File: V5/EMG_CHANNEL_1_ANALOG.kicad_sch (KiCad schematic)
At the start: 38 parts, among them J301 AudioJack3 TRS, U301 INA333xxDGK, U302 MCP6004

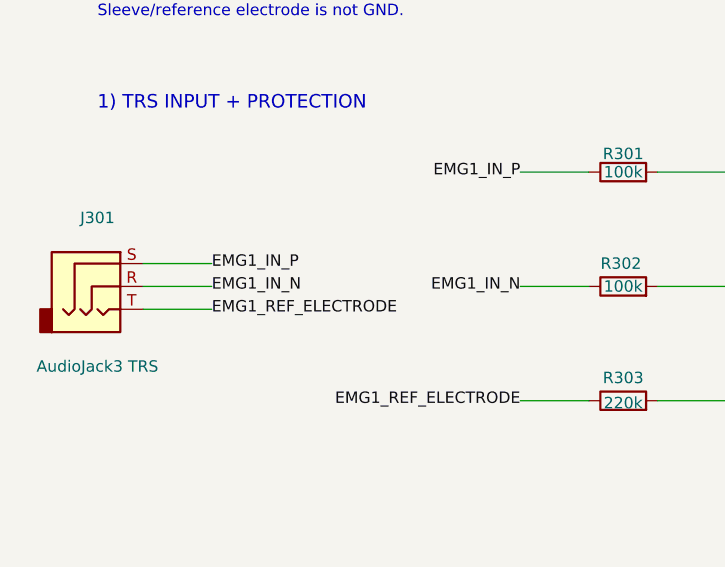
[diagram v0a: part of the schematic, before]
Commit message: fix trs electrode terminal mapping
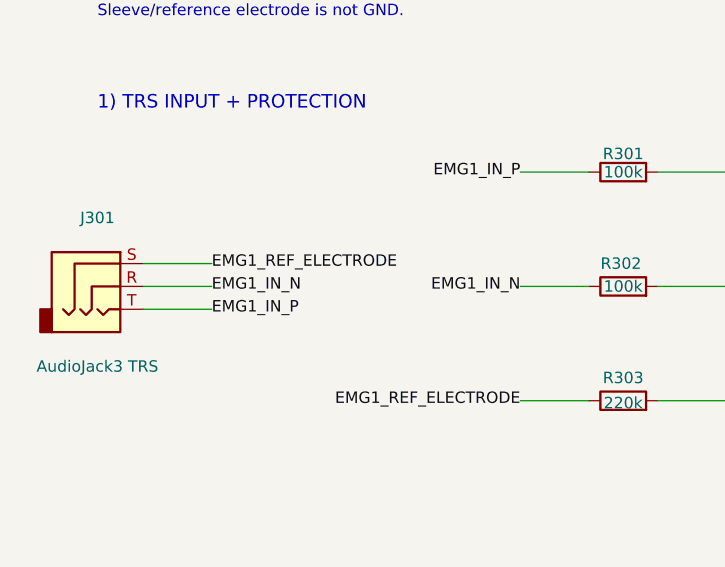
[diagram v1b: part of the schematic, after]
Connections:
- net EMG1_IN_P: now also J301.T; no longer J301.S
- net EMG1_REF_ELECTRODE: now also J301.S; no longer J301.T
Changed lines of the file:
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@@
 		)
 	)
-	(label "EMG1_IN_P"
+	(label "EMG1_REF_ELECTRODE"
 		(at 38.1 66.04 0)
 		(effects
@@
 		)
 	)
-	(label "EMG1_REF_ELECTRODE"
+	(label "EMG1_IN_P"
 		(at 38.1 71.12 0)
 		(effects

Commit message: assign mirrored analog footprint batch
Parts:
- C310, C311, C314: footprint (none) -> Capacitor_SMD:C_0603_1608Metric
- R311, R312, R313, R314, R321, R331, R341, R351: footprint (none) -> Resistor_SMD:R_0805_2012Metric
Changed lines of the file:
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@@
 			)
 		)
-		(property "Footprint" ""
+		(property "Footprint" "Capacitor_SMD:C_0603_1608Metric"
 			(at 195.58 58.42 0)
 			(hide yes)
@@
 			)
 		)
-		(property "Footprint" ""
+		(property "Footprint" "Capacitor_SMD:C_0603_1608Metric"
 			(at 246.38 73.66 0)
 			(hide yes)
@@
 			)
 		)
-		(property "Footprint" ""
+		(property "Footprint" "Resistor_SMD:R_0805_2012Metric"
 			(at 292.1 88.9 0)
 			(hide yes)
@@
 			)
 		)
-		(property "Footprint" ""
+		(property "Footprint" "Resistor_SMD:R_0805_2012Metric"
 			(at 302.26 107.95 0)
 			(hide yes)
@@
 			)
 		)
-		(property "Footprint" ""
+		(property "Footprint" "Resistor_SMD:R_0805_2012Metric"
 			(at 322.58 55.88 0)
 			(hide yes)
@@
 			)
 		)
-		(property "Footprint" ""
+		(property "Footprint" "Resistor_SMD:R_0805_2012Metric"
 			(at 365.76 73.66 0)
 			(hide yes)
@@
 			)
 		)
-		(property "Footprint" ""
+		(property "Footprint" "Capacitor_SMD:C_0603_1608Metric"
 			(at 434.34 78.74 0)
 			(hide yes)
@@
 			)
 		)
-		(property "Footprint" ""
+		(property "Footprint" "Resistor_SMD:R_0805_2012Metric"
 			(at 274.32 229.87 0)
 			(hide yes)
@@
 			)
 		)
-		(property "Footprint" ""
+		(property "Footprint" "Resistor_SMD:R_0805_2012Metric"
 			(at 438.15 57.15 0)
 			(hide yes)
@@
 			)
 		)
-		(property "Footprint" ""
+		(property "Footprint" "Resistor_SMD:R_0805_2012Metric"
 			(at 439.42 93.98 0)
 			(hide yes)
@@
 			)
 		)
-		(property "Footprint" ""
+		(property "Footprint" "Resistor_SMD:R_0805_2012Metric"
 			(at 436.88 119.38 0)
 			(hide yes)

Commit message: select and assign analog ic packages
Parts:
- U301: value INA333xxDGK -> INA333AIDGKT; footprint (none) -> Package_SO:VSSOP-8_3x3mm_P0.65mm
- U302: value MCP6004 -> MCP6004-I/SL; footprint Package_DIP:DIP-14_W7.62mm -> Package_SO:SOIC-14_3.9x8.7mm_P1.27mm
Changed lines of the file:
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@@
 			)
 		)
-		(property "Value" "INA333xxDGK"
+		(property "Value" "INA333AIDGKT"
 			(at 196.85 90.17 0)
 			(show_name no)
@@
 			)
 		)
-		(property "Footprint" ""
+		(property "Footprint" "Package_SO:VSSOP-8_3x3mm_P0.65mm"
 			(at 210.82 73.66 0)
 			(hide yes)
@@
 			)
 		)
-		(property "Value" "MCP6004"
+		(property "Value" "MCP6004-I/SL"
 			(at 322.58 80.518 0)
 			(show_name no)
@@
 			)
 		)
-		(property "Footprint" "Package_DIP:DIP-14_W7.62mm"
+		(property "Footprint" "Package_SO:SOIC-14_3.9x8.7mm_P1.27mm"
 			(at 322.58 73.66 0)
 			(hide yes)
@@
 			)
 		)
-		(property "Value" "MCP6004"
+		(property "Value" "MCP6004-I/SL"
 			(at 337.82 165.1 0)
 			(show_name no)
@@
 			)
 		)
-		(property "Footprint" "Package_DIP:DIP-14_W7.62mm"
+		(property "Footprint" "Package_SO:SOIC-14_3.9x8.7mm_P1.27mm"
 			(at 337.82 157.48 0)
 			(hide yes)
@@
 			)
 		)
-		(property "Value" "MCP6004"
+		(property "Value" "MCP6004-I/SL"
 			(at 337.312 236.982 0)
 			(show_name no)
@@
 			)
 		)
-		(property "Footprint" "Package_DIP:DIP-14_W7.62mm"
+		(property "Footprint" "Package_SO:SOIC-14_3.9x8.7mm_P1.27mm"
 			(at 337.82 229.87 0)
 			(hide yes)
@@
 			)
 		)
-		(property "Value" "MCP6004"
+		(property "Value" "MCP6004-I/SL"
 			(at 278.384 313.436 0)
 			(show_name no)
@@
 			)
 		)
-		(property "Footprint" "Package_DIP:DIP-14_W7.62mm"
+		(property "Footprint" "Package_SO:SOIC-14_3.9x8.7mm_P1.27mm"
 			(at 278.13 306.07 0)
 			(hide yes)
@@
 			)
 		)
-		(property "Value" "MCP6004"
+		(property "Value" "MCP6004-I/SL"
 			(at 419.608 178.054 0)
 			(show_name no)
@@
 			)
 		)
-		(property "Footprint" "Package_DIP:DIP-14_W7.62mm"
+		(property "Footprint" "Package_SO:SOIC-14_3.9x8.7mm_P1.27mm"
 			(at 420.37 165.1 0)
 			(hide yes)

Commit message: assign analog input filter footprints
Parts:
- C301, C302, C303: footprint (none) -> Capacitor_SMD:C_0603_1608Metric
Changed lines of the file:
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@@
 			)
 		)
-		(property "Footprint" ""
+		(property "Footprint" "Capacitor_SMD:C_0603_1608Metric"
 			(at 130.81 134.62 0)
 			(hide yes)
@@
 			)
 		)
-		(property "Footprint" ""
+		(property "Footprint" "Capacitor_SMD:C_0603_1608Metric"
 			(at 130.81 104.14 0)
 			(hide yes)
@@
 			)
 		)
-		(property "Footprint" ""
+		(property "Footprint" "Capacitor_SMD:C_0603_1608Metric"
 			(at 168.91 95.25 0)
 			(hide yes)

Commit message: retain footprints for optional dnp filters
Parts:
- C304: footprint (none) -> Capacitor_SMD:C_0603_1608Metric
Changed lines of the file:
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@@
 			)
 		)
-		(property "Footprint" ""
+		(property "Footprint" "Capacitor_SMD:C_0603_1608Metric"
 			(at 130.81 118.11 0)
 			(hide yes)

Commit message: select and assign mechanical interface parts
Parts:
- J301: value AudioJack3 TRS -> SJ1-3523N; footprint (none) -> Connector_Audio:Jack_3.5mm_CUI_SJ1-3523N_Horizontal
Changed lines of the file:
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@@
 			)
 		)
-		(property "Value" "AudioJack3 TRS"
+		(property "Value" "SJ1-3523N"
 			(at 25.4 77.47 0)
 			(show_name no)
@@
 			)
 		)
-		(property "Footprint" ""
+		(property "Footprint" "Connector_Audio:Jack_3.5mm_CUI_SJ1-3523N_Horizontal"
 			(at 25.4 68.58 0)
 			(hide yes)

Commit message: assign final resistor footprints
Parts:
- R301, R302, R303, R304, R305, R306: footprint (none) -> Resistor_SMD:R_1206_3216Metric
- R307: footprint (none) -> Resistor_SMD:R_0805_2012Metric
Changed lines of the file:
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@@
 			)
 		)
-		(property "Footprint" ""
+		(property "Footprint" "Resistor_SMD:R_1206_3216Metric"
 			(at 83.82 55.88 0)
 			(hide yes)
@@
 			)
 		)
-		(property "Footprint" ""
+		(property "Footprint" "Resistor_SMD:R_1206_3216Metric"
 			(at 83.82 68.58 0)
 			(hide yes)
@@
 			)
 		)
-		(property "Footprint" ""
+		(property "Footprint" "Resistor_SMD:R_1206_3216Metric"
 			(at 83.82 81.28 0)
 			(hide yes)
@@
 			)
 		)
-		(property "Footprint" ""
+		(property "Footprint" "Resistor_SMD:R_1206_3216Metric"
 			(at 130.81 57.15 0)
 			(hide yes)
@@
 			)
 		)
-		(property "Footprint" ""
+		(property "Footprint" "Resistor_SMD:R_1206_3216Metric"
 			(at 130.81 72.39 0)
 			(hide yes)
@@
 			)
 		)
-		(property "Footprint" ""
+		(property "Footprint" "Resistor_SMD:R_1206_3216Metric"
 			(at 130.81 87.63 0)
 			(hide yes)
@@
 			)
 		)
-		(property "Footprint" ""
+		(property "Footprint" "Resistor_SMD:R_0805_2012Metric"
 			(at 168.91 73.66 0)
 			(hide yes)

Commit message: Place EMG V5 PCB blocks and fix analog feedback nets
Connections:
- net RAW_GAIN_FB: now also U302.2 (-); no longer U302.3 (+)
- net RAW_HPF_NODE: now also U302.3 (+); no longer U302.2 (-)
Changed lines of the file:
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@@
 		)
 	)
-	(label "RAW_HPF_NODE"
+	(label "RAW_GAIN_FB"
 		(at 304.8 76.2 180)
 		(effects
@@
 		)
 	)
-	(label "RAW_GAIN_FB"
+	(label "RAW_HPF_NODE"
 		(at 304.8 71.12 180)
 		(effects
@@
 		)
 	)
-	(embedded_fonts no)
 )
